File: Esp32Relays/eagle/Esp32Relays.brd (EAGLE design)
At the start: 54.4 x 16.6 mm, 20 parts, among them J1 Audio2, J3 AUDIO_JACK_3.5MM_PTH, J4 AUDIO_JACK_3.5MM_PTH, U1 CD4066BE

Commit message: Changed cap values and some labels
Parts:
- removed C5: 2.2uF, SparkFun-Capacitors:0805
- removed J5: (no value), SparkFun-Connectors:1X03
- added AJ-IN: AUDIO_JACK_3.5MM_PTH, SparkFun-Connectors:AUDIO-JACK
- added C2: 1uF, SparkFun-Capacitors:0805
- C1, C3, C4: value 2.2uF -> 1uF
- J3: value AUDIO_JACK_3.5MM_PTH -> (none); device SparkFun-Connectors:AUDIO-JACK -> SparkFun-Connectors:1X03
- R3: value 4.7k -> 100k
- R4: value 100k -> 4.7k
- moved C3 12.0 mm to (21.5, 9.59)
- moved J3 9.27 mm to (41.5, 10.2), turned to 270 degrees
- moved R3 8.19 mm to (29.3, 7.05)
- moved R4 7.75 mm to (37.1, 7.11)
- moved R1 2.60 mm to (37.1, 9.72)
- moved C4 2.54 mm to (21.5, 7.05)
- moved R5 2.54 mm to (25.1, 7.05)
- moved R6 2.54 mm to (25.1, 9.59)
- renumbered J4 to AJ-OUT
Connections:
- net 3V3: now also J3.2, R1.1; no longer J5.2, R3.1
- net A1-SIG-OUT: now also C3.2, R5.2; no longer C4.2, R6.2
- net A1IN: now also AJ-IN.RING, AJ-IN.RSH; no longer J3.RING, J3.RSH
- net A1OUT: now also C3.1; no longer C4.1
- net B1-SIG-IN: now also C2.2, R3.2; no longer C3.2, R4.2
- net B1-SIG-OUT: now also C4.2, R6.2; no longer C5.2, R5.2
- net B1IN: now also AJ-IN.TIP, AJ-IN.TSH, C2.1; no longer C3.1, J3.TIP, J3.TSH
- net B1OUT: now also C4.1; no longer C5.1
- net D26: now also J3.3; no longer J5.3
- net GND: now also AJ-IN.SLEEVE, J3.1, R4.2; no longer J3.SLEEVE, J5.1, R1.2
- net N$2: now also R1.2, R3.1; no longer R1.1, R3.2
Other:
- board text added: "Audio OUT"

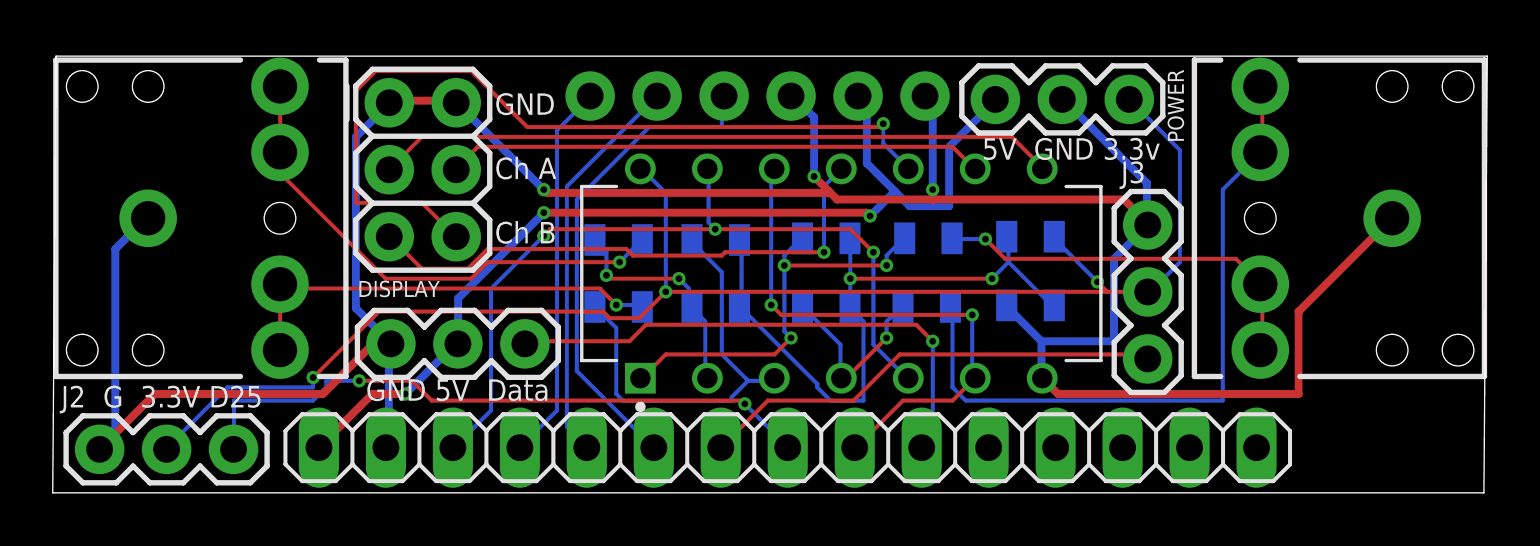
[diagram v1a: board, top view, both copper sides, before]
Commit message: Added brightness GPIO
and removed - unused - Touch IRQ pin
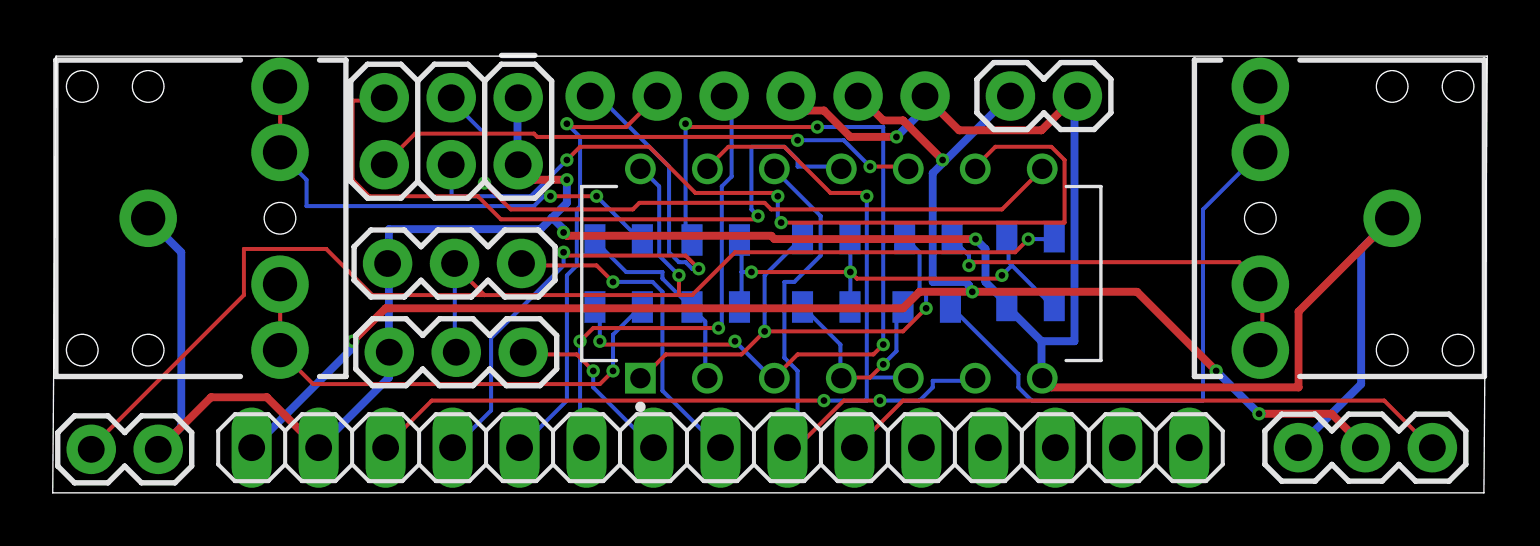
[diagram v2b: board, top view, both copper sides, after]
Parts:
- removed POWER: (no value), SparkFun-Connectors:1X03
- added 3V3-IN, 5V-IN: (no value), SparkFun-Connectors:1X02
- moved DISPLAY 34.6 mm to (47.2, 1.71)
- moved J3 29.2 mm to (12.8, 5.33), turned to 0 degrees
- moved J2 13.0 mm to (12.7, 8.70)
- moved J1 4.89 mm to (17.7, 15.0), turned to 180 degrees
- moved ESP32-RIGHT 2.55 mm to (25.3, 1.71)
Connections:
- net 3V3: now also 3V3-IN.1; no longer POWER.1
- net GND: now also 3V3-IN.2, 5V-IN.2; no longer POWER.2
- net VIN: now also 5V-IN.1; no longer POWER.3
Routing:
- net VIN: track 38.2 -> 61.6 mm, vias 3 -> 5
- net B1-SIG-OUT: track 16.4 -> 33.7 mm, vias 0 -> 5
- net A2OUT: track 20.4 -> 33.3 mm, vias 0 -> 3
- net D25: track 24.4 -> 12.6 mm, vias 2 -> 1
- net B2OUT: track 31.9 -> 20.9 mm, vias 1 -> 2
- net D26: track 17.7 -> 6.83 mm, vias 0 -> 1
- net D12: track 14.4 -> 23.3 mm, vias 0 -> 2
- net B2IN: track 20.9 -> 27.0 mm
- net N$2: track 24.9 -> 19.2 mm, vias 2 -> 3
- net D13: track 30.2 -> 35.5 mm, vias 3 -> 2
- net 3V3: track 56.8 -> 52.8 mm, vias 3 -> 2
- net GND: track 110.9 -> 114.2 mm, vias 3 -> 4
- net A1-SIG-IN: track 15.7 -> 19.1 mm, vias 3 -> 2
- net D32: track 20.2 -> 23.4 mm, vias 1 -> 0
- net D14: track 15.1 -> 17.4 mm, vias 0 -> 1
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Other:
- board text added: "Audio 2"
- board text added: "Data 5V GND"
- board text added: "ESP32 Neopixel v2"
- board text added: "GND 3v3"
- board text added: "GND 5v"
- board text added: "OUT IN"
- board text removed: "5V GND 3.3v"
- board text removed: "ESP32 Neopixel v1.0"
- board text removed: "G 3.3V D25"
- board text removed: "GND 5V Data"
